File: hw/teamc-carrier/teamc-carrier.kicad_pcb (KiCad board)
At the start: 2 copper layers, 65 x 56 mm, 5 parts, among them J1 GPIO

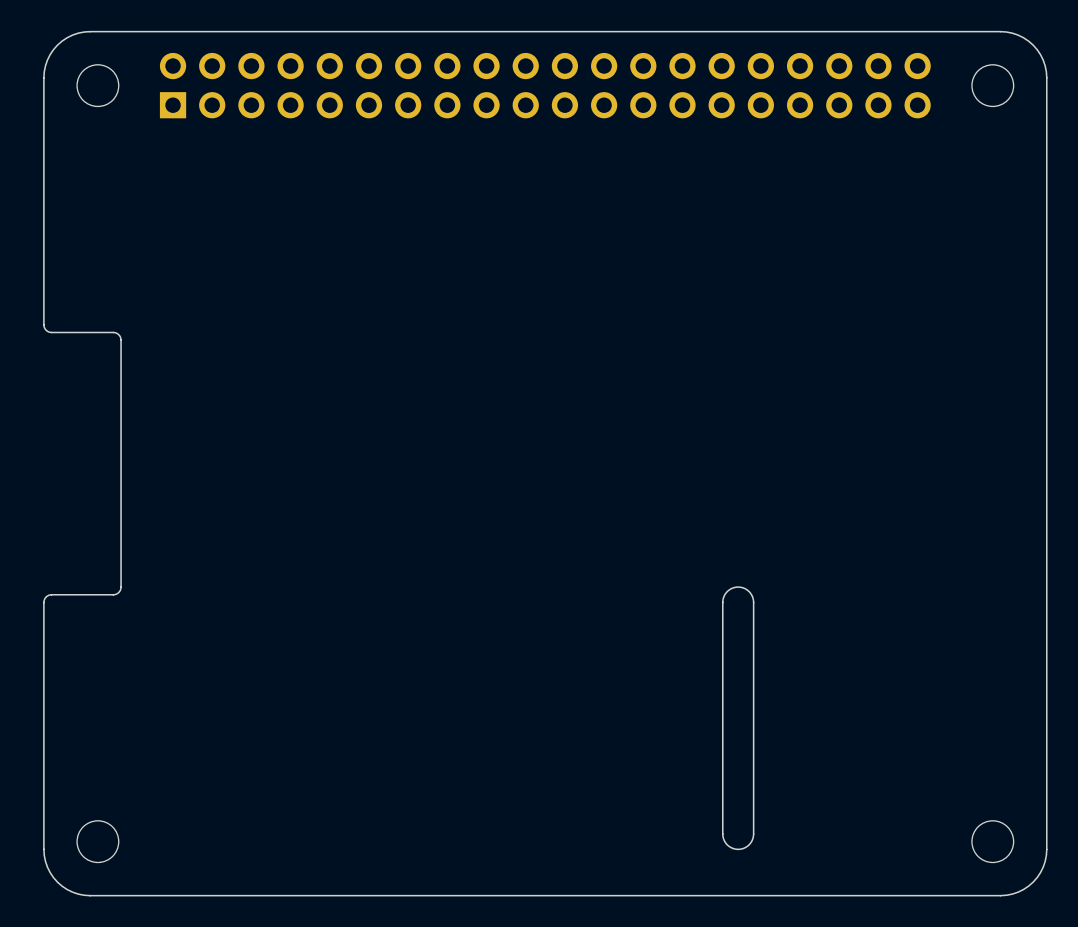
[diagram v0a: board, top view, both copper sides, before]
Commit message: carrier: review fixes (Si2333DDS, BCM857BS, fuse, soft start, D_SMF, pull-ups to 3V3_PI, MODE->VIN), power+SPI routed (DRC 0 errors), GND vias, BoM, design notes; CLAUDE.md session log
Co-Authored-By: Claude Opus 5.5 <noreply@anthropic.com>
Claude-Session: https://claude.ai/code/session_01Dy4TuRNF8V28KreA3jwCtM
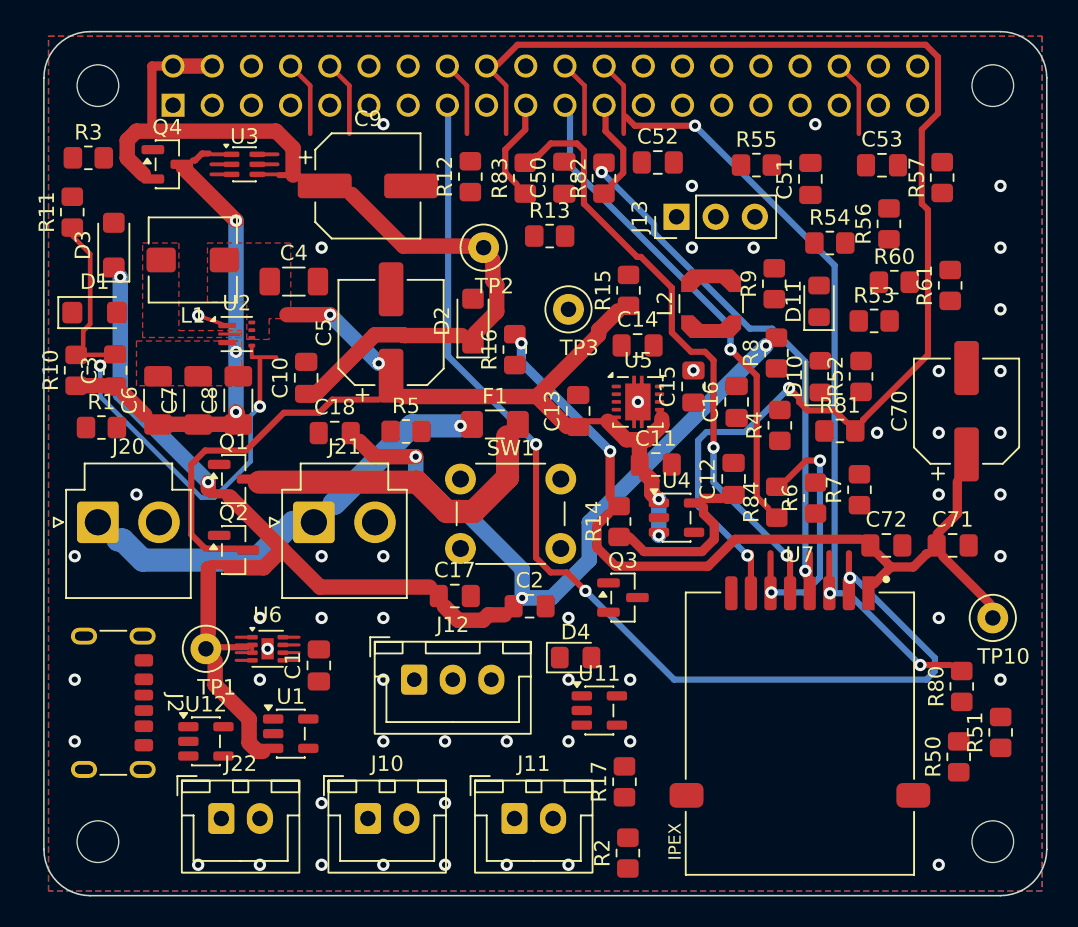
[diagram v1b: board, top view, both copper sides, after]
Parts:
- added C1: 10u 25V X5R, Capacitor_SMD:C_0805_2012Metric_Pad1.18x1.45mm_HandSolder, F.Cu at (117.8, 85.1)
- added C10: 100n 50V X7R, Capacitor_SMD:C_0805_2012Metric_Pad1.18x1.45mm_HandSolder, F.Cu at (117.0, 66.4)
- added C11: 10u 25V X5R, Capacitor_SMD:C_0805_2012Metric_Pad1.18x1.45mm_HandSolder, F.Cu at (139.7, 72.1)
- added C12: 1u 16V X7R, Capacitor_SMD:C_0805_2012Metric_Pad1.18x1.45mm_HandSolder, F.Cu at (144.7, 73.0)
- added C13: 10u 25V X5R, Capacitor_SMD:C_0805_2012Metric_Pad1.18x1.45mm_HandSolder, F.Cu at (134.6, 68.6)
- added C14: 10u 25V X5R, Capacitor_SMD:C_0805_2012Metric_Pad1.18x1.45mm_HandSolder, F.Cu at (138.5, 64.3)
- added C15: 10u 25V X5R, Capacitor_SMD:C_0805_2012Metric_Pad1.18x1.45mm_HandSolder, F.Cu at (142.1, 67.0)
- added C16: 100n 50V X7R, Capacitor_SMD:C_0805_2012Metric_Pad1.18x1.45mm_HandSolder, F.Cu at (144.9, 68.0)
- added C17: 100n 50V X7R, Capacitor_SMD:C_0805_2012Metric_Pad1.18x1.45mm_HandSolder, F.Cu at (126.6, 80.6)
- added C18: 100n 50V X7R, Capacitor_SMD:C_0805_2012Metric_Pad1.18x1.45mm_HandSolder, F.Cu at (118.8, 70.0)
- added C2: 10u 25V X5R, Capacitor_SMD:C_0805_2012Metric_Pad1.18x1.45mm_HandSolder, F.Cu at (131.5, 81.2)
- added C3: 100p 50V C0G, Capacitor_SMD:C_0805_2012Metric_Pad1.18x1.45mm_HandSolder, F.Cu at (104.6, 66.0)
- added C4: 22u 25V X5R, Capacitor_SMD:C_1206_3216Metric_Pad1.33x1.80mm_HandSolder, F.Cu at (116.2, 60.2)
- added C5: 100u 16V, Capacitor_SMD:CP_Elec_6.3x5.4, F.Cu at (122.5, 63.5)
- added C50: 100n X7R, Capacitor_SMD:C_0805_2012Metric_Pad1.18x1.45mm_HandSolder, F.Cu at (133.7, 53.5)
- added C51: 100n X7R, Capacitor_SMD:C_0805_2012Metric_Pad1.18x1.45mm_HandSolder, F.Cu at (149.7, 53.5)
- added C52: 100n X7R, Capacitor_SMD:C_0805_2012Metric_Pad1.18x1.45mm_HandSolder, F.Cu at (139.8, 52.5)
- added C53: 100n X7R, Capacitor_SMD:C_0805_2012Metric_Pad1.18x1.45mm_HandSolder, F.Cu at (154.3, 52.7)
- added C6: 22u 25V X5R, Capacitor_SMD:C_1206_3216Metric_Pad1.33x1.80mm_HandSolder, F.Cu at (107.4, 67.9)
- added C7: 22u 25V X5R, Capacitor_SMD:C_1206_3216Metric_Pad1.33x1.80mm_HandSolder, F.Cu at (110.0, 67.9)
- added C70: 100u 10V, Capacitor_SMD:CP_Elec_6.3x5.4, F.Cu at (159.8, 68.6)
- added C71: 10u X5R, Capacitor_SMD:C_0805_2012Metric_Pad1.18x1.45mm_HandSolder, F.Cu at (158.9, 77.3)
- added C72: 100n X7R, Capacitor_SMD:C_0805_2012Metric_Pad1.18x1.45mm_HandSolder, F.Cu at (154.6, 77.3)
- added C8: 22u 25V X5R, Capacitor_SMD:C_1206_3216Metric_Pad1.33x1.80mm_HandSolder, F.Cu at (112.6, 67.9)
- added C9: 100u 16V, Capacitor_SMD:CP_Elec_6.3x5.4, F.Cu at (121.0, 54.0)
- added D1: SMF5.0A, Diode_SMD:D_SMF, F.Cu at (103.3, 62.2)
- added D10: green, LED_SMD:LED_0805_2012Metric_Pad1.15x1.40mm_HandSolder, F.Cu at (150.3, 66.4)
- added D11: red, LED_SMD:LED_0805_2012Metric_Pad1.15x1.40mm_HandSolder, F.Cu at (150.2, 61.5)
- added D2: SMF5.0A, Diode_SMD:D_SMF, F.Cu at (127.8, 62.8)
- added D3: SMF5.0A, Diode_SMD:D_SMF, F.Cu at (104.5, 57.8)
- added D4: red CHG, LED_SMD:LED_0805_2012Metric_Pad1.15x1.40mm_HandSolder, F.Cu at (134.5, 84.6)
- added F1: 5A fast, Fuse:Fuse_1206_3216Metric_Pad1.42x1.75mm_HandSolder, F.Cu at (129.2, 69.5)
- added J10: GO/STOP button, Connector_JST:JST_XH_B2B-XH-A_1x02_P2.50mm_Vertical, F.Cu at (121.0, 95.0)
- added J11: role toggle, Connector_JST:JST_XH_B2B-XH-A_1x02_P2.50mm_Vertical, F.Cu at (130.5, 95.0)
- added J12: mode toggle, Connector_JST:JST_XH_B3B-XH-A_1x03_P2.50mm_Vertical, F.Cu at (124.0, 86.0)
- added J13: UART console, Connector_PinHeader_2.54mm:PinHeader_1x03_P2.54mm_Vertical, F.Cu at (141.0, 56.0)
- added J2: USB-C charge, Connector_USB:USB_C_Receptacle_GCT_USB4125-xx-x-0190_6P_TopMnt_Horizontal, F.Cu at (103.4, 87.5)
- added J20: BATT 18650, Connector_JST:JST_VH_B2P-VH_1x02_P3.96mm_Vertical, F.Cu at (103.5, 75.8)
- added J21: BATT 2 (DNP), Connector_JST:JST_VH_B2P-VH_1x02_P3.96mm_Vertical, F.Cu at (117.5, 75.8)
- added J22: PWR toggle, Connector_JST:JST_XH_B2B-XH-A_1x02_P2.50mm_Vertical, F.Cu at (111.5, 95.0)
- added L1: 1u Isat 11.5A, Inductor_SMD:L_Wuerth_HCI-5040, F.Cu at (109.7, 58.8)
- added L2: 2u2, Inductor_SMD:L_Coilcraft_LPS4018, F.Cu at (143.2, 61.6)
- added Q1: Si2333DDS, Package_TO_SOT_SMD:SOT-23, F.Cu at (112.3, 73.0)
- added Q2: Si2333DDS, Package_TO_SOT_SMD:SOT-23, F.Cu at (112.3, 77.6)
- added Q3: 2N7002, Package_TO_SOT_SMD:SOT-23, F.Cu at (137.5, 80.7)
- added Q4: AO3401A, Package_TO_SOT_SMD:SOT-23, F.Cu at (108.0, 52.6)
- added R1: 10k 1%, Resistor_SMD:R_0805_2012Metric_Pad1.20x1.40mm_HandSolder, F.Cu at (103.7, 69.7)
- added R10: 750k 1%, Resistor_SMD:R_0805_2012Metric_Pad1.20x1.40mm_HandSolder, F.Cu at (102.1, 66.0)
- added R11: 100k 1%, Resistor_SMD:R_0805_2012Metric_Pad1.20x1.40mm_HandSolder, F.Cu at (101.8, 55.7)
- added R12: 10k 1%, Resistor_SMD:R_0805_2012Metric_Pad1.20x1.40mm_HandSolder, F.Cu at (127.6, 53.4)
- added R13: 47k 1%, Resistor_SMD:R_0805_2012Metric_Pad1.20x1.40mm_HandSolder, F.Cu at (132.8, 57.2)
- added R14: 0R (fit), Resistor_SMD:R_0805_2012Metric_Pad1.20x1.40mm_HandSolder, F.Cu at (137.3, 75.8)
- added R15: 100R, Resistor_SMD:R_0805_2012Metric_Pad1.20x1.40mm_HandSolder, F.Cu at (137.9, 60.8)
- added R16: 0R (DNP), Resistor_SMD:R_0805_2012Metric_Pad1.20x1.40mm_HandSolder, F.Cu at (130.5, 64.6)
- added R17: 10k 1%, Resistor_SMD:R_0805_2012Metric_Pad1.20x1.40mm_HandSolder, F.Cu at (137.6, 92.6)
- added R2: 5k1 1%, Resistor_SMD:R_0805_2012Metric_Pad1.20x1.40mm_HandSolder, F.Cu at (137.8, 97.2)
- added R3: 5k1 1%, Resistor_SMD:R_0805_2012Metric_Pad1.20x1.40mm_HandSolder, F.Cu at (102.9, 52.2)
- added R4: 2k21 1%, Resistor_SMD:R_0805_2012Metric_Pad1.20x1.40mm_HandSolder, F.Cu at (147.7, 69.5)
- added R5: 1k 1%, Resistor_SMD:R_0805_2012Metric_Pad1.20x1.40mm_HandSolder, F.Cu at (123.5, 69.9)
- added R50: 10k, Resistor_SMD:R_0805_2012Metric_Pad1.20x1.40mm_HandSolder, F.Cu at (159.3, 91.0)
- added R51: 10k, Resistor_SMD:R_0805_2012Metric_Pad1.20x1.40mm_HandSolder, F.Cu at (162.0, 89.4)
- added R52: 10k, Resistor_SMD:R_0805_2012Metric_Pad1.20x1.40mm_HandSolder, F.Cu at (153.0, 66.3)
- added R53: 10k, Resistor_SMD:R_0805_2012Metric_Pad1.20x1.40mm_HandSolder, F.Cu at (153.8, 62.8)
- added R54: 1k, Resistor_SMD:R_0805_2012Metric_Pad1.20x1.40mm_HandSolder, F.Cu at (150.9, 57.7)
- added R55: 1k, Resistor_SMD:R_0805_2012Metric_Pad1.20x1.40mm_HandSolder, F.Cu at (146.2, 52.6)
- added R56: 1k, Resistor_SMD:R_0805_2012Metric_Pad1.20x1.40mm_HandSolder, F.Cu at (154.8, 56.5)
- added R57: 1k, Resistor_SMD:R_0805_2012Metric_Pad1.20x1.40mm_HandSolder, F.Cu at (158.2, 53.5)
- added R6: 100k 1%, Resistor_SMD:R_0805_2012Metric_Pad1.20x1.40mm_HandSolder, F.Cu at (150.0, 74.2)
- added R60: 330, Resistor_SMD:R_0805_2012Metric_Pad1.20x1.40mm_HandSolder, F.Cu at (155.1, 60.2)
- added R61: 330, Resistor_SMD:R_0805_2012Metric_Pad1.20x1.40mm_HandSolder, F.Cu at (158.7, 60.5)
- added R7: 10k 1%, Resistor_SMD:R_0805_2012Metric_Pad1.20x1.40mm_HandSolder, F.Cu at (152.9, 73.7)
- added R8: 100k 1%, Resistor_SMD:R_0805_2012Metric_Pad1.20x1.40mm_HandSolder, F.Cu at (147.5, 64.8)
- added R80: 10k, Resistor_SMD:R_0805_2012Metric_Pad1.20x1.40mm_HandSolder, F.Cu at (159.5, 86.4)
- added R81: 10k, Resistor_SMD:R_0805_2012Metric_Pad1.20x1.40mm_HandSolder, F.Cu at (151.6, 69.9)
- added R82: 33, Resistor_SMD:R_0805_2012Metric_Pad1.20x1.40mm_HandSolder, F.Cu at (136.3, 53.5)
- added R83: 33, Resistor_SMD:R_0805_2012Metric_Pad1.20x1.40mm_HandSolder, F.Cu at (131.2, 53.5)
- added R84: 33, Resistor_SMD:R_0805_2012Metric_Pad1.20x1.40mm_HandSolder, F.Cu at (147.5, 74.5)
- added R9: 10k 1%, Resistor_SMD:R_0805_2012Metric_Pad1.20x1.40mm_HandSolder, F.Cu at (147.3, 60.3)
- added SW1: bench GO/STOP, Button_Switch_THT:SW_PUSH_6mm, F.Cu at (127.0, 73.0)
- added TP1: VBAT, TestPoint:TestPoint_Loop_D2.50mm_Drill1.0mm, F.Cu at (110.5, 84.0)
- added TP10: 3V3_RADIO, TestPoint:TestPoint_Loop_D2.50mm_Drill1.0mm, F.Cu at (161.5, 82.0)
- added TP2: 5V_PI, TestPoint:TestPoint_Loop_D2.50mm_Drill1.0mm, F.Cu at (128.5, 58.0)
- added TP3: GND, TestPoint:TestPoint_Loop_D2.50mm_Drill1.0mm, F.Cu at (134.0, 62.0)
- added U1: MCP73831, Package_TO_SOT_SMD:SOT-23-5, F.Cu at (116.0, 89.5)
- added U11: SP0504BAHTG, Package_TO_SOT_SMD:SOT-23-5, F.Cu at (136.0, 88.0)
- added U12: SP0504BAHTG, Package_TO_SOT_SMD:SOT-23-5, F.Cu at (110.5, 90.0)
- added U2: TPS61022, Package_DFN_QFN:Texas_RWU0007A_VQFN-7_2x2mm_P0.5mm, F.Cu at (112.5, 63.6)
- added U3: BCM857BS, Package_TO_SOT_SMD:SOT-363_SC-70-6, F.Cu at (113.0, 52.6)
- added U4: TLV75533, Package_TO_SOT_SMD:SOT-23-5, F.Cu at (141.0, 75.5)
- added U5: TPS63001, Package_SON:Texas_DRC0010J, F.Cu at (138.5, 68.0)
- added U6: MAX17048, teamc:MAX17048_TDFN-8-1EP_2x2mm, F.Cu at (114.5, 84.0)
- added U7: E01-ML01SP4, teamc:E01-ML01SP4, F.Cu at (149.0, 89.5)
- J1: value GPIO -> RPi 3 A+ GPIO; footprint Connector_PinSocket_2.54mm:PinSocket_2x20_P2.54mm_Vertical -> teamc:PinSocket_2x20_P2.54mm_Vertical_Pad1.5mm
- MH1, MH2, MH3, MH4: value MountingHole_2.7mm_M2.5 -> M2.5
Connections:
- net +5V renamed 5V_PI
- J1 pad 1: +3V3 -> unconnected-(J1-Pin_1-Pad1)
- J1 pad 10: /GPIO15/RXD0 -> UART_RX
- J1 pad 11: /GPIO17 -> BTN_TXRX
- J1 pad 12: /GPIO18/PCM.CLK -> unconnected-(J1-Pin_12-Pad12)
- J1 pad 13: /GPIO27 -> SW_ROLE
- J1 pad 15: /GPIO22 -> RADIO_CE
- J1 pad 16: /GPIO23 -> SW_MODE_NM
- J1 pad 17: +3V3 -> 3V3_PI
- J1 pad 18: /GPIO24 -> RADIO_IRQ
- J1 pad 19: /GPIO10/SPI0.MOSI -> SPI_MOSI
- J1 pad 21: /GPIO9/SPI0.MISO -> SPI_MISO
- J1 pad 22: /GPIO25 -> FG_ALRT
- J1 pad 23: /GPIO11/SPI0.SCLK -> SPI_SCK
- J1 pad 24: /GPIO8/SPI0.CE0 -> RADIO_CSN
- J1 pad 26: /GPIO7/SPI0.CE1 -> unconnected-(J1-Pin_26-Pad26)
- J1 pad 27: /ID_SDA -> unconnected-(J1-Pin_27-Pad27)
- J1 pad 28: /ID_SCL -> unconnected-(J1-Pin_28-Pad28)
- J1 pad 29: /GPIO5 -> LED_ACT
- J1 pad 3: /GPIO2/SDA1 -> I2C_SDA
- J1 pad 31: /GPIO6 -> LED_STATUS
- J1 pad 32: /GPIO12/PWM0 -> unconnected-(J1-Pin_32-Pad32)
- J1 pad 33: /GPIO13/PWM1 -> unconnected-(J1-Pin_33-Pad33)
- J1 pad 35: /GPIO19/PCM.FS -> unconnected-(J1-Pin_35-Pad35)
- J1 pad 36: /GPIO16 -> SW_MODE_MRM
- J1 pad 37: /GPIO26 -> CHG_STAT
- J1 pad 38: /GPIO20/PCM.DIN -> unconnected-(J1-Pin_38-Pad38)
- J1 pad 40: /GPIO21/PCM.DOUT -> unconnected-(J1-Pin_40-Pad40)
- J1 pad 5: /GPIO3/SCL1 -> I2C_SCL
- J1 pad 7: /GPIO4/GPCLK0 -> unconnected-(J1-Pin_7-Pad7)
- J1 pad 8: /GPIO14/TXD0 -> UART_TX
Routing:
- net VBAT: track 0.00 -> 96.0 mm, vias 0 -> 5
- net RADIO_IRQ: track 0.00 -> 83.7 mm, vias 0 -> 2
- net RADIO_CE: track 0.00 -> 71.4 mm, vias 0 -> 3
- net VBAT_SW: track 0.00 -> 59.7 mm, vias 0 -> 4
- net RADIO_CSN: track 0.00 -> 56.0 mm, vias 0 -> 3
- net 5V_PI: track 0.00 -> 52.0 mm
- net 3V3_RADIO: track 0.00 -> 46.9 mm, vias 0 -> 2
- net /radio/MOSI_R: track 0.00 -> 38.6 mm, vias 0 -> 2
- net /radio/SCK_R: track 0.00 -> 35.1 mm, vias 0 -> 2
- net /power/FB: track 0.00 -> 33.9 mm, vias 0 -> 2
- net SPI_MISO: track 0.00 -> 30.8 mm, vias 0 -> 1
- net /power/5V_BOOST: track 0.00 -> 24.5 mm, vias 0 -> 3
- net /power/BAT_IN: track 0.00 -> 23.2 mm, vias 0 -> 1
- net /power/BAT_RAW: track 0.00 -> 20.4 mm
- net /radio/MISO_R: track 0.00 -> 16.4 mm, vias 0 -> 2
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- added copper zone on F.Cu, net /power/5V_BOOST
- added copper zone on F.Cu, net /power/SW_NODE
- added copper zone on B.Cu, net GND
- added copper zone on F.Cu, net GND
- added copper zone on F.Cu, net VBAT_SW
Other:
- outline, holes or cut-outs redrawn
- board text added: "HAT ON: never plug the Pi's micro-USB"
- board text added: "Team C Pi 3 A+ HAT - DRAFT for ET review - 19-Oct-26"
- board text removed: "CAMERA (OPTIONAL)"
- board text removed: "DISPLAY (OPTIONAL)"
- board text removed: "Extend PCB edge 0.5mm if using SMT header"
- board text removed: "PoE"
- board text removed: "RJ45"
- board text removed: "USB"

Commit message: carrier: re-placed in clusters, boost GND pocket fixed, SP4 keep-out on both layers, power+SPI routed (DRC 0 errors); small nets handed to ET; JLCPCB-class 0.2 mm rules
- removed SW1 (bench button), J21 (2nd cell -> harness), D1 (VBUS ESD on U12's spare channel)
- router: rip-up/reroute + negotiated congestion options (neither finished the small nets at 0.3 mm)
- design notes: hand-off list for ET, fab rules, layout-driven changes; BoM ~EUR 102/device

Co-Authored-By: Claude Opus 5.5 <noreply@anthropic.com>
Claude-Session: https://claude.ai/code/session_01Dy4TuRNF8V28KreA3jwCtM
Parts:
- removed D1: SMF5.0A, Diode_SMD:D_SMF
- removed J21: BATT 2 (DNP), Connector_JST:JST_VH_B2P-VH_1x02_P3.96mm_Vertical
- removed SW1: bench GO/STOP, Button_Switch_THT:SW_PUSH_6mm
- moved R9 41.6 mm to (118.5, 90.4), turned to 0 degrees
- moved R3 37.8 mm to (109.6, 89.4), turned to 90 degrees
- moved TP1 34.9 mm to (138.2, 62.9)
- moved R80 33.8 mm to (139.1, 59.4), turned to 0 degrees
- moved R17 33.8 mm to (143.7, 59.4), turned to 0 degrees
- moved R55 32.5 mm to (129.4, 80.5), turned to 90 degrees
- moved R4 31.3 mm to (119.6, 83.4), turned to 0 degrees
- moved R2 30.1 mm to (110.5, 84.6), turned to 0 degrees
- moved R13 28.7 mm to (104.3, 53.8), turned to 90 degrees
- moved R54 27.7 mm to (132.9, 78.8)
- moved D3 25.9 mm to (120.6, 78.2), turned to 0 degrees
- moved R8 25.7 mm to (125.3, 77.9), turned to 0 degrees
- moved R51 25.4 mm to (137.7, 82.1), turned to 0 degrees
- moved R52 24.9 mm to (133.1, 81.3), turned to 0 degrees
- moved D2 23.4 mm to (104.4, 63.6)
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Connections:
- U12 pad 5: unconnected-(U12-K-Pad5) -> VBUS_USB
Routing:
- net /power/FB: track 33.9 -> 10.3 mm, vias 2 -> 0
- net VBAT: track 96.0 -> 72.9 mm, vias 5 -> 1
- net /power/BAT_IN: track 23.2 -> 2.91 mm, vias 1 -> 0
- net RADIO_IRQ: track 83.7 -> 63.7 mm
- net RADIO_CE: track 71.4 -> 52.4 mm, vias 3 -> 1
- net /power/BAT_RAW: track 20.4 -> 2.35 mm
- net /radio/MISO_R: track 16.4 -> 6.72 mm, vias 2 -> 0
- net RADIO_CSN: track 56.0 -> 47.9 mm, vias 3 -> 2
- net 3V3_RADIO: track 46.9 -> 39.2 mm
- net SPI_MISO: track 30.8 -> 38.4 mm
- net 5V_PI: track 52.0 -> 44.9 mm, vias 0 -> 4
- net VBAT_SW: track 59.7 -> 64.7 mm, vias 4 -> 7
- net /power/ZVD_B: track 3.94 -> 6.26 mm
- net /radio/MOSI_R: track 38.6 -> 36.5 mm
- net /power/BB_OUT: track 0.00 -> 1.80 mm
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
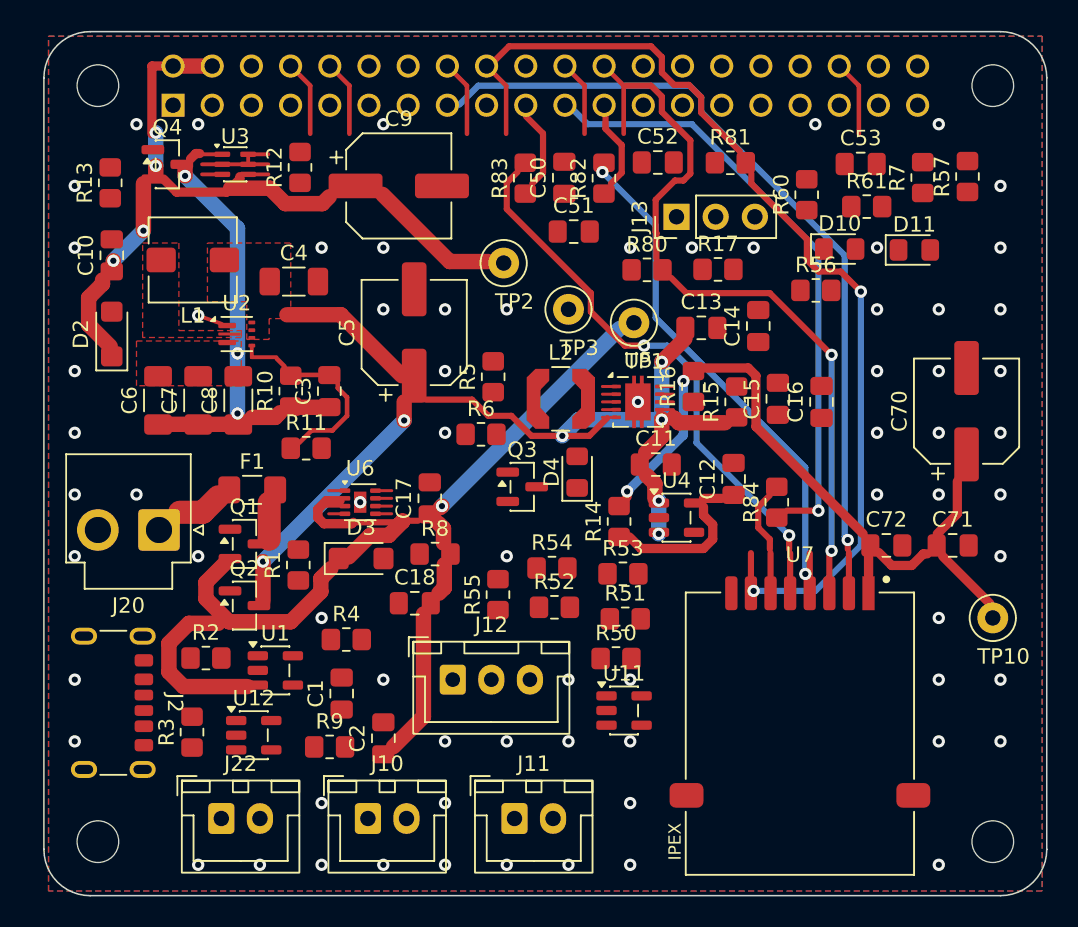
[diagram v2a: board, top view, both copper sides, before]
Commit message: carrier: routing finished (0 unconnected); Freerouting + finishing pass; 3D models and render script
- net classes: only real power nets wide (/power/* caught gate/LED nets at 1 mm); PowerFine/FinePitch split,
  Ground class (ignored by the autorouter)
- autoroute_carrier.py: Freerouting via Specctra DSN/SES, merge of the autorouted nets only, padded
  clearances, GND stitching + KiCad-connectivity island links
- finish_carrier.py: the few boxed-in pins by hand (EP ties, FG_ALRT escape, L2 turned, C15 turned,
  3V3_RADIO via moved, R15 feed rerouted), grid router from existing copper, ground passes, dangling clean-up
- 3D: fetch_3d.py, teamc.3dshapes (SP4, MAX17048, JST-VH, simplified Pi 3 A+), render_board.py
- silk_carrier.py, fab_carrier.py (not run yet)

Co-Authored-By: Claude Opus 5.5 <noreply@anthropic.com>
Claude-Session: https://claude.ai/code/session_01Y7mBamiGXo4bnsmXC1gZLM
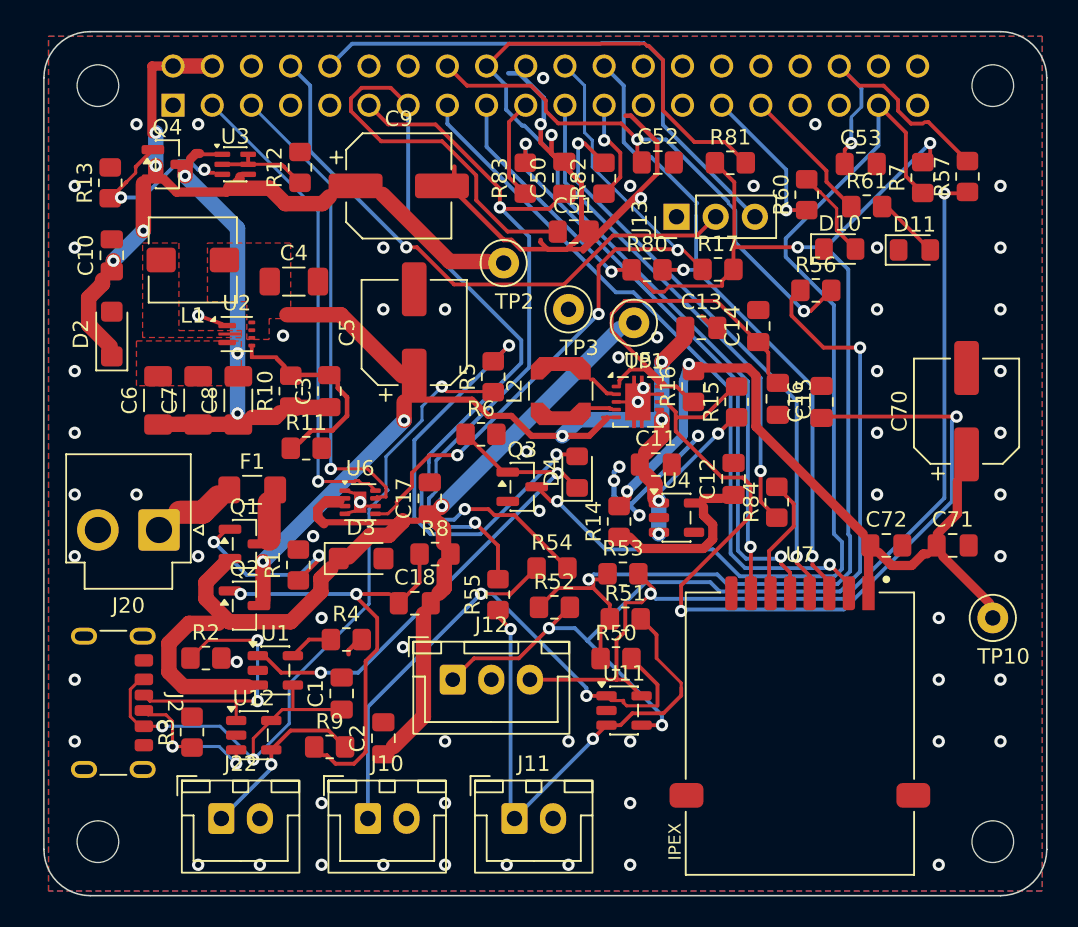
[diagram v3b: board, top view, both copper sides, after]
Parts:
- moved L2 0.50 mm to (133.5, 67.3), turned to 90 degrees
- turned C15 to -90 degrees
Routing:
- net 3V3_PI: track 0.00 -> 98.4 mm, vias 0 -> 4
- net GND: track 6.59 -> 76.4 mm, vias 70 -> 71
- net CHG_STAT: track 0.00 -> 63.3 mm, vias 0 -> 1
- net SW_ROLE: track 0.00 -> 63.3 mm, vias 0 -> 1
- net /ui/SW_MODE_NM_J: track 0.00 -> 62.9 mm, vias 0 -> 3
- net /ui/SW_MODE_MRM_J: track 0.00 -> 59.7 mm, vias 0 -> 2
- net /power/BB_VINA: track 0.90 -> 56.6 mm, vias 0 -> 2
- net VBUS_USB: track 0.00 -> 54.3 mm, vias 0 -> 3
- net BTN_TXRX: track 0.00 -> 50.8 mm, vias 0 -> 2
- net /ui/BTN_TXRX_J: track 0.00 -> 40.5 mm, vias 0 -> 2
- net FG_ALRT: track 5.97 -> 46.1 mm, vias 0 -> 3
- net /ui/SW_ROLE_J: track 0.00 -> 34.2 mm, vias 0 -> 2
- net /power/CHG_STAT_RAW: track 0.00 -> 33.9 mm, vias 0 -> 2
- net UART_TX: track 4.92 -> 37.7 mm, vias 0 -> 1
- net SW_MODE_NM: track 4.92 -> 35.3 mm, vias 0 -> 2
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
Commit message: carrier rev A: DRC 0/0/0, silkscreen, 3D models applied, fab outputs; hw page v0.7; docs
- silk_carrier.py: 59 references on the silkscreen at 1.0/0.8 mm, 26 on F.Fab; bottom text rev A 21-Oct-26
- render_board.py --apply-models on both boards (SP4, MAX17048, JST-VH bodies; substitutes for models missing
  upstream); renders top/bottom/iso + HAT on the Pi 3 A+
- fab_carrier.py: gerbers, Excellon drill + maps, KiCad pos + JLCPCB CPL (DNP out), assembly + copper PDFs, BoM,
  teamc-carrier_gerbers.zip
- SP4 breakout: U1 refreshed from the library (it gained its 3D model): DRC 0 again
- DESIGN_NOTES: routing pipeline, net classes, state on 21-Oct with 5 review points for ET; CLAUDE.md, README
- hw page v0.7 republished (same URL); PDF in briefs/ (v0.6 removed)

Co-Authored-By: Claude Opus 5.5 <noreply@anthropic.com>
Claude-Session: https://claude.ai/code/session_01Y7mBamiGXo4bnsmXC1gZLM
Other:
- board text added: "Team C Pi 3 A+ HAT - rev A for ET review - 21-Oct-26"
- board text removed: "Team C Pi 3 A+ HAT - DRAFT for ET review - 19-Oct-26"
